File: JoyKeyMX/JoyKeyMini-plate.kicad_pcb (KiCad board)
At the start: 2 copper layers, 93 x 51 mm, 21 parts, among them J1 DB9_Female, SW1 SW_WITHLED, SW3 SW_WITHLED, SW4 SW_WITHLED, SW5 SW_WITHLED, SW6 SW_WITHLED

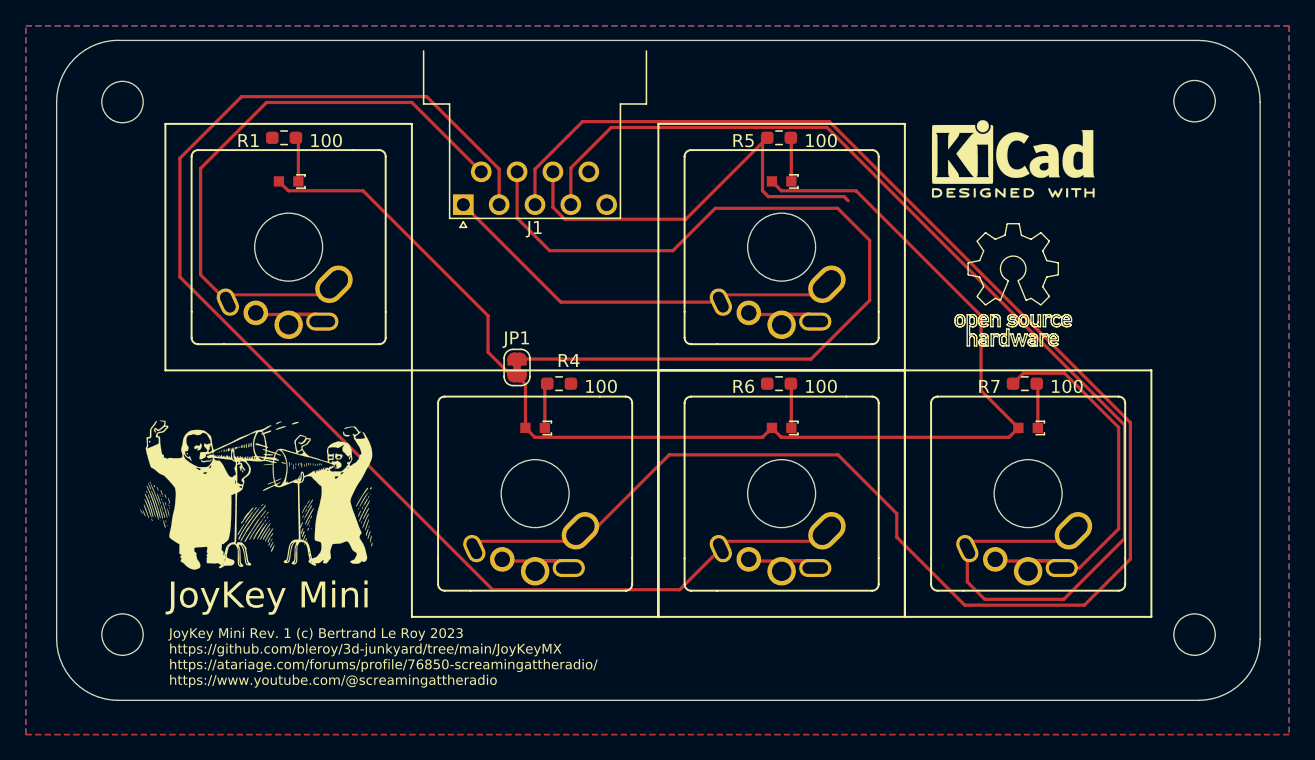
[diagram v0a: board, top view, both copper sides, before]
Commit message: JoyKey Mini case and plate
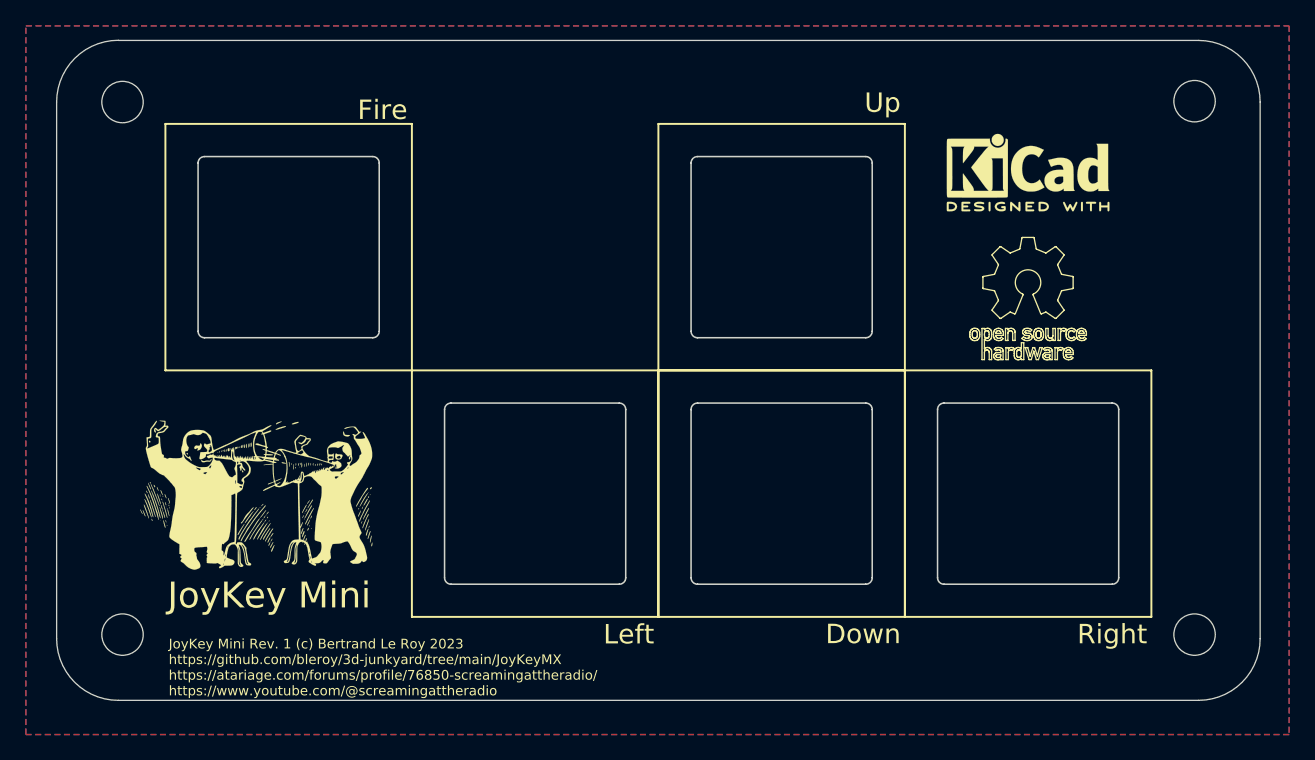
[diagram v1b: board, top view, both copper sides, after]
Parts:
- removed the ? at (63.9, 26.6)
- removed J1: DB9_Female, Connector_Dsub:DSUB-9_Female_Horizontal_P2.77x2.54mm_EdgePinOffset9.40mm
- removed JP1: SolderJumper_2_Bridged, Jumper:SolderJumper-2_P1.3mm_Bridged_RoundedPad1.0x1.5mm
- removed R1, R4, R5, R6, R7: 100, Resistor_SMD:R_0603_1608Metric_Pad0.98x0.95mm_HandSolder
- SW1, SW3, SW4, SW5, SW6: footprint Library:MX-1-00U-LED -> Library:SW_Hole_1.00u_PCB
- moved REF** 1.56 mm to (96.5, 33.6)
- moved REF** 1.56 mm to (96.5, 42.1)
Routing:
- net 3: track 121.8 -> 0.00 mm
- net LED_VCC: track 99.8 -> 0.00 mm
- net 2: track 94.0 -> 0.00 mm
- net 4: track 82.5 -> 0.00 mm
- net 7: track 68.0 -> 0.00 mm
- net 8: track 57.2 -> 0.00 mm
- net 6: track 37.2 -> 0.00 mm
- net 1: track 23.0 -> 0.00 mm
- net Net-(R6-Pad2): track 3.38 -> 0.00 mm
- net Net-(R5-Pad2): track 3.33 -> 0.00 mm
- net Net-(R7-Pad2): track 3.33 -> 0.00 mm
- net Net-(R4-Pad2): track 3.23 -> 0.00 mm
- net Net-(R1-Pad2): track 3.18 -> 0.00 mm
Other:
- board text added: "Down"
- board text added: "Fire"
- board text added: "Left"
- board text added: "Right"
- board text added: "Up"
